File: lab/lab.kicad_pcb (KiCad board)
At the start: 2 copper layers, 45.7 x 31.8 mm, 42 parts, among them J1 FACE, J3 C?, Q1 Q_NPN_EBC, Q2 Q_NPN_EBC, Q3 Q_NPN_EBC, U1 LM324, U2 L78L33_TO92

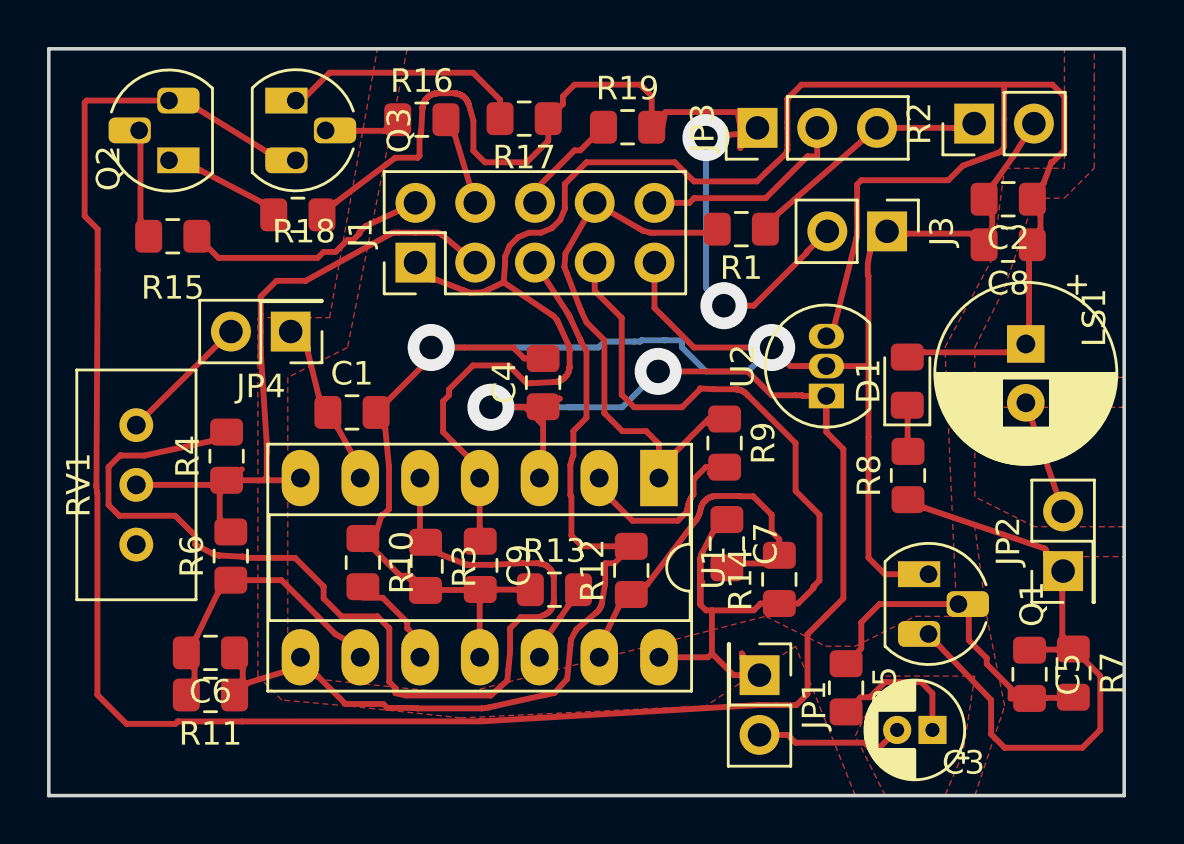
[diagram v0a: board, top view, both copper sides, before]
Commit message: Turned IC to bask
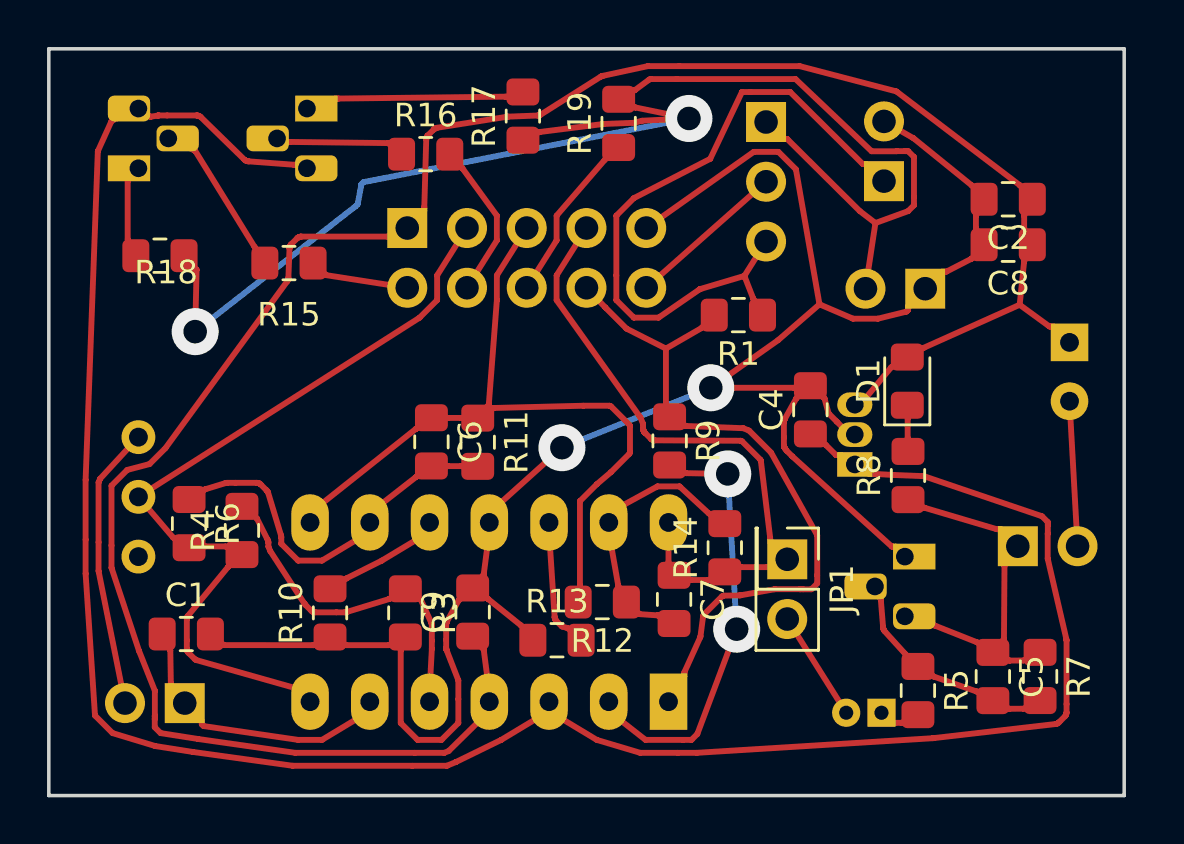
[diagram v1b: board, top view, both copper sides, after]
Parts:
- C3, J1, J3, JP2, JP3, JP4, LS1, Q1, Q2, Q3, R2, RV1, U1, U2: moved to B.Cu
- moved JP4 16.4 mm to (24.8, 45.6)
- moved R11 15.6 mm to (37.3, 34.5), turned to 270 degrees
- moved C6 13.0 mm to (35.3, 34.5), turned to 270 degrees
- moved C1 11.8 mm to (24.9, 42.7)
- moved C4 11.4 mm to (51.4, 33.1)
- moved U1 9.52 mm to (45.4, 45.5), turned to 90 degrees
- moved R18 6.12 mm to (23.8, 26.6)
- moved R15 5.07 mm to (29.3, 26.9)
- moved JP1 5.07 mm to (50.4, 39.5)
- moved R2 4.55 mm to (54.6, 23.4), turned to 0 degrees
- moved R1 3.66 mm to (48.4, 29.1)
- moved C7 3.26 mm to (45.6, 41.2)
- moved R4 3.23 mm to (27.3, 38.3)
- moved U2 3.15 mm to (53.3, 35.5)
- moved R5 3.06 mm to (56.0, 45.1)
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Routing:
- net Net-(R3-Pad1): track 43.9 -> 14.9 mm
- net CMEAS: track 45.0 -> 64.8 mm
- net TMEAS: track 10.6 -> 28.8 mm
- net SIN: track 41.7 -> 27.5 mm
- net Net-(C5-Pad1): track 27.2 -> 16.3 mm
- net Net-(R9-Pad2): track 8.65 -> 18.6 mm, vias 0 -> 2
- net +5V: track 86.3 -> 95.7 mm
- net 3V3: track 106.0 -> 97.9 mm, vias 2 -> 0
- net TRIANGLE: track 40.3 -> 32.9 mm
- net Net-(JP4-Pad2): track 5.66 -> 12.1 mm
- net CSD1: track 10.5 -> 4.24 mm
- net GNDD: track 85.9 -> 91.9 mm
- net SQUARE: track 29.3 -> 35.0 mm
- net Net-(C1-Pad1): track 7.06 -> 12.4 mm
- net Net-(C5-Pad2): track 14.1 -> 9.73 mm
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- removed copper zone on F.Cu, net +5V
- removed copper zone on F.Cu, net 3V3
- removed copper zone on F.Cu, net GNDD
- removed copper zone on F.Cu, net Net-(C3-Pad1)
- removed copper zone on F.Cu, net Net-(C5-Pad1)
- removed copper zone on F.Cu, net Net-(JP2-Pad2)

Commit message: Final PCB
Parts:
- moved R18 5.44 mm to (21.6, 21.6), turned to 270 degrees
- moved R8 3.95 mm to (59.5, 35.7)
- moved D1 3.40 mm to (58.9, 31.7)
- moved U2 3.39 mm to (56.7, 35.5)
- moved C4 1.98 mm to (53.4, 33.3)
- moved R9 1.57 mm to (43.9, 34.2)
- moved Q2 1.27 mm to (24.1, 22.9)
- moved R12 0.48 mm to (42.2, 41.1)
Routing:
- net CMEAS: track 64.8 -> 41.1 mm, vias 2 -> 0
- net TMEAS: track 28.8 -> 14.4 mm
- net +5V: track 95.7 -> 109.1 mm
- net Net-(R3-Pad1): track 14.9 -> 26.8 mm
- net SQUARE: track 35.0 -> 42.3 mm, vias 0 -> 2
- net 3V3: track 97.9 -> 91.3 mm, vias 0 -> 3
- net CSD1: track 4.24 -> 10.7 mm
- net TRIANGLE: track 32.9 -> 26.5 mm
- net GNDD: track 91.9 -> 98.3 mm, vias 2 -> 0
- net Net-(C7-Pad2): track 12.0 -> 16.3 mm
- net Net-(R9-Pad2): track 18.6 -> 14.7 mm, vias 2 -> 0
- net VREF3.3: track 30.0 -> 33.8 mm, vias 0 -> 2
- net Net-(C1-Pad1): track 12.4 -> 15.8 mm
- net MEAS: track 6.80 -> 10.2 mm
- net Net-(C5-Pad1): track 16.3 -> 13.3 mm
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- added copper zone on F.Cu, net +5V
- added copper zone on F.Cu, net 3V3
- added copper zone on F.Cu, net GNDD
- added copper zone on F.Cu, net TRIANGLE
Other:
- net class Default: clearance 0.2 -> 0.25; trace_width 0.25 -> 0.35; via_dia 2 -> 1.2; via_drill 1 -> 0.8
- rule trace_clearance: 0.2 -> 0.25

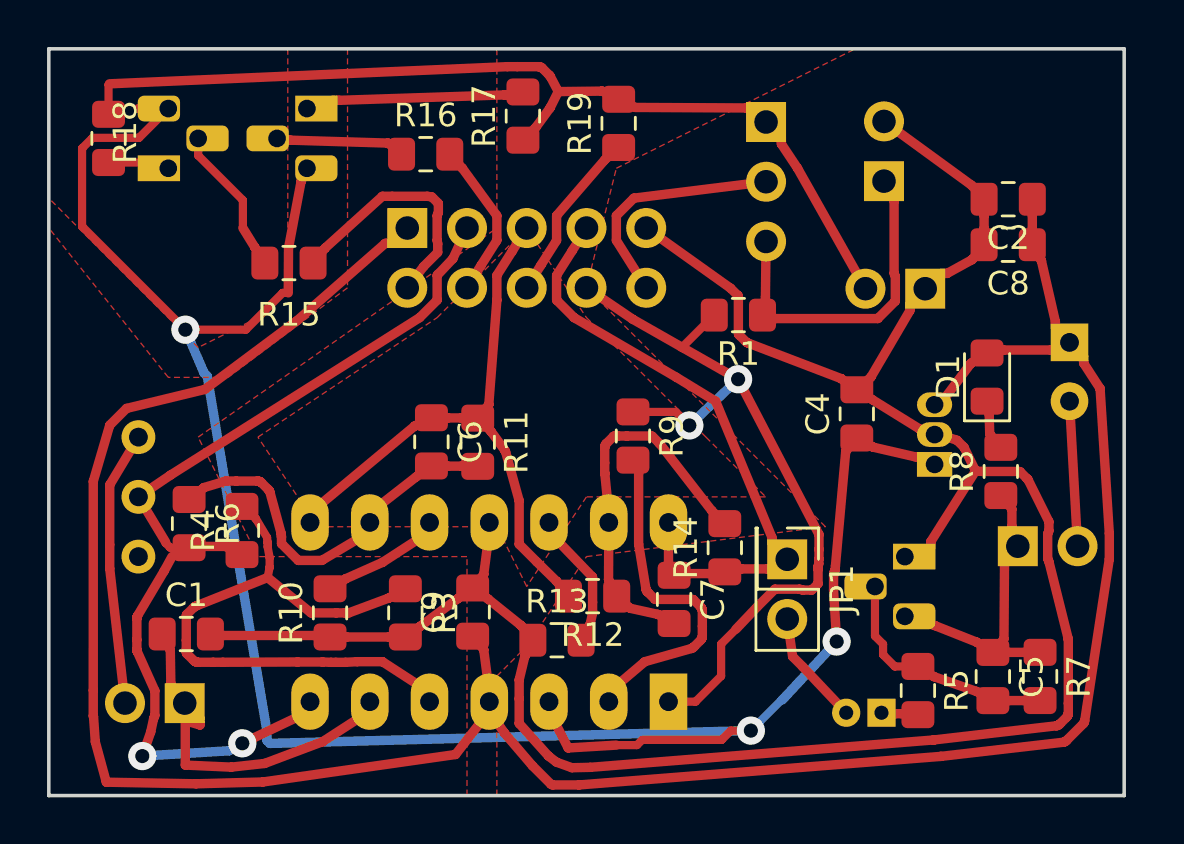
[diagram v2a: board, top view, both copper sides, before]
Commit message: Fill more space with Cu.
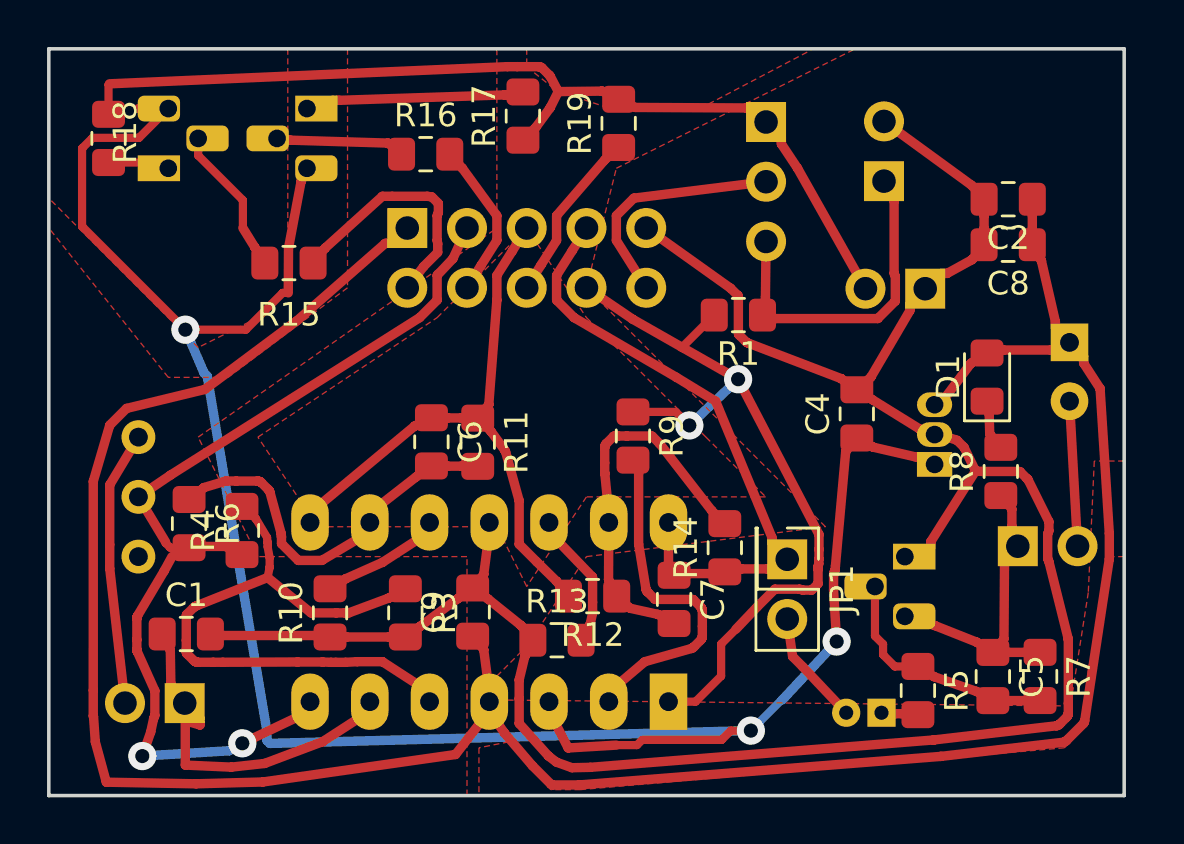
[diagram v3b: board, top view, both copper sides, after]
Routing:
- added copper zone on F.Cu, net CMEAS
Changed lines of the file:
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@@
       (pts
         (xy 38.1 45.72) (xy 38.1 44.45) (xy 39.37 43.18) (xy 41.91 39.37) (xy 52.07 38.1)
-        (xy 41.91 27.94) (xy 43.18 22.86) (xy 53.34 17.78) (xy 64.77 17.78) (xy 64.77 49.53)
-        (xy 38.1 49.53)
+        (xy 41.91 27.94) (xy 43.18 22.86) (xy 53.34 17.78) (xy 64.77 17.78) (xy 64.77 35.306)
+        (xy 63.5 35.306) (xy 63.246 40.894) (xy 62.484 45.72) (xy 38.1 45.466)
       )
     )
@@
       )
     )
+  )
+  (zone (net 3) (net_name +5V) (layer F.Cu) (hatch edge 0.508)
+    (connect_pads (clearance 0.508))
+    (min_thickness 0.254)
+    (fill yes (arc_segments 16) (thermal_gap 0.508) (thermal_bridge_width 0.508))
+    (polygon
+      (pts
+        (xy 64.77 44.196) (xy 64.77 39.37) (xy 64.262 39.37) (xy 63.246 44.196) (xy 62.992 46.736)
+        (xy 62.23 47.498) (xy 41.656 49.276) (xy 40.386 49.276) (xy 38.608 47.244) (xy 37.338 47.498)
+        (xy 37.338 49.53) (xy 64.77 49.53)
+      )
+    )
+  )
+  (zone (net 26) (net_name CMEAS) (layer F.Cu) (hatch edge 0.508)
+    (connect_pads (clearance 0.508))
+    (min_thickness 0.254)
+    (fill yes (arc_segments 16) (thermal_gap 0.508) (thermal_bridge_width 0.508))
+    (polygon
+      (pts
+        (xy 46.736 20.32) (xy 51.562 17.78) (xy 39.37 17.78) (xy 39.37 18.542) (xy 40.64 19.558)
+        (xy 42.926 20.32)
+      )
+    )

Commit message: Removed wrong parts. Remade PCB. Too thick.
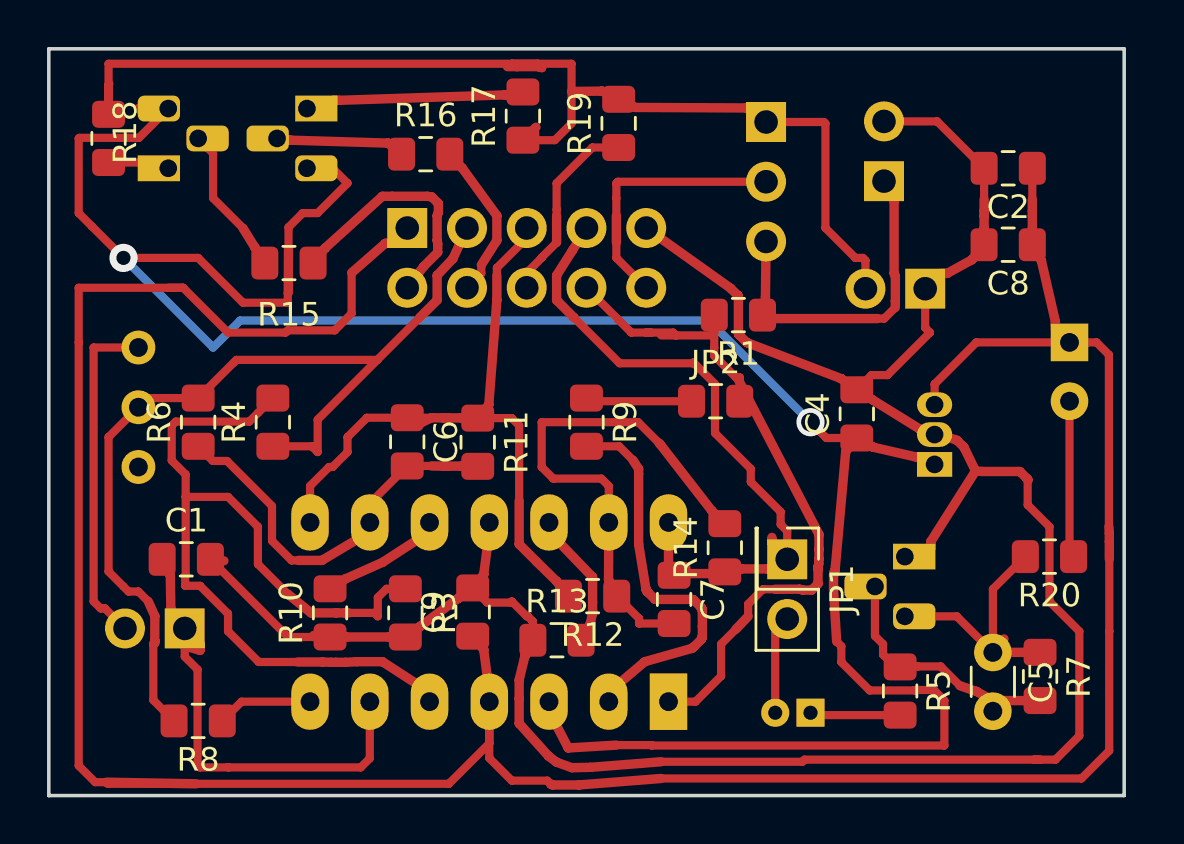
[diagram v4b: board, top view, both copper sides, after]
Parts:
- removed D1: LED, Diode_SMD:D_0805_2012Metric_Pad1.15x1.40mm_HandSolder
- added R20: 0R, Resistor_SMD:R_0805_2012Metric_Pad1.15x1.40mm_HandSolder, F.Cu at (61.6, 39.4)
- C5: footprint Capacitor_SMD:C_0805_2012Metric_Pad1.15x1.40mm_HandSolder -> Capacitor_THT:C_Disc_D3.0mm_W1.6mm_P2.50mm
- JP2: value SPK -> 0R; footprint Connector_PinHeader_2.54mm:PinHeader_2x01_P2.54mm_Vertical -> Resistor_SMD:R_0805_2012Metric_Pad1.15x1.40mm_HandSolder; moved to F.Cu
- R8: value 1K -> 0R
- moved R8 35.7 mm to (25.4, 46.4), turned to 180 degrees
- moved JP2 14.3 mm to (47.4, 32.8)
- moved R4 4.79 mm to (28.6, 33.7)
- moved R6 4.33 mm to (25.4, 33.7), turned to 90 degrees
- moved RV1 3.81 mm to (22.9, 30.5)
- moved C1 3.18 mm to (24.9, 39.5)
- moved JP4 3.17 mm to (24.8, 42.4)
- moved C3 3.02 mm to (51.4, 46.0)
- moved R9 2.06 mm to (41.9, 33.7)
- moved C2 1.32 mm to (59.8, 22.9)
- moved C6 1.03 mm to (34.3, 34.5)
- moved C5 1.02 mm to (59.2, 43.4)
- moved R5 0.76 mm to (55.2, 45.1)
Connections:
- JP2 pad 1: Net-(C5-Pad1) -> VREF3.3
- JP2 pad 2: Net-(JP2-Pad2) -> VREF3.3
- LS1 pad 2: Net-(JP2-Pad2) -> Net-(LS1-Pad2)
- R8 pad 1: Net-(C5-Pad1) -> SQUARE
- R8 pad 2: Net-(D1-Pad1) -> SQUARE
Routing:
- net +5V: track 109.1 -> 130.3 mm
- net Net-(R3-Pad1): track 26.8 -> 38.1 mm
- net CMEAS: track 41.1 -> 50.8 mm
- net 3V3: track 91.3 -> 100.9 mm, vias 3 -> 2
- net GNDD: track 98.3 -> 107.6 mm
- net Net-(LS1-Pad2): track 0.00 -> 6.68 mm
- net Net-(C7-Pad2): track 16.3 -> 22.7 mm
- net Net-(JP2-Pad2): track 6.17 -> 0.00 mm
- net Net-(C1-Pad1): track 15.8 -> 21.1 mm
- net TRIANGLE: track 26.5 -> 31.8 mm
- net Net-(C3-Pad1): track 1.55 -> 4.50 mm
- net Net-(JP4-Pad2): track 11.7 -> 14.5 mm
- net Net-(C6-Pad2): track 16.6 -> 19.3 mm
- net SIN: track 26.2 -> 28.9 mm
- net SQUARE: track 42.3 -> 45.0 mm, vias 2 -> 0
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- removed copper zone on F.Cu, net +5V
- removed copper zone on F.Cu, net 3V3
- removed copper zone on F.Cu, net CMEAS
- removed copper zone on F.Cu, net GNDD
- removed copper zone on F.Cu, net TRIANGLE

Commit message: Added thick tracks.
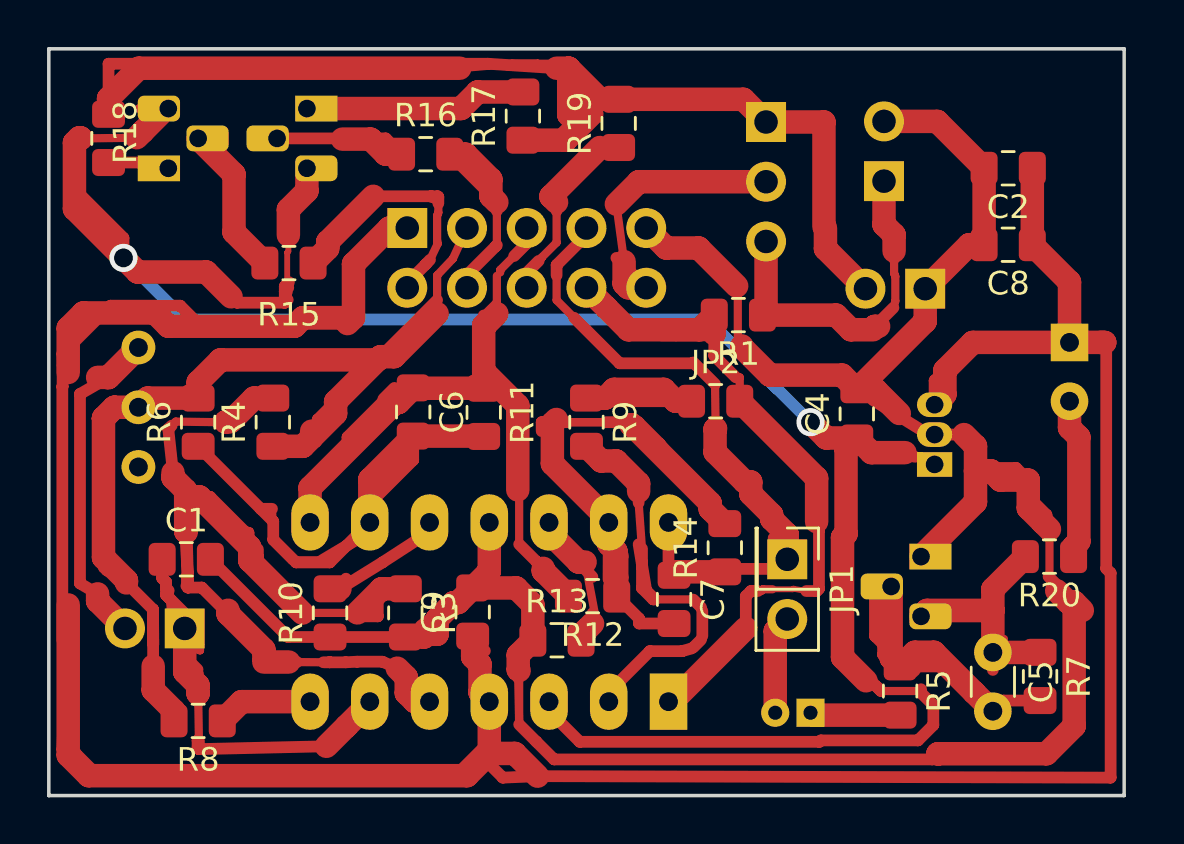
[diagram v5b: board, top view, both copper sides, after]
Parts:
- moved C6 1.30 mm to (34.5, 33.2)
- moved R11 1.30 mm to (37.5, 33.2)
- moved Q1 0.69 mm to (56.1, 39.4)
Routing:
- net CMEAS: track 50.8 -> 103.6 mm
- net +5V: track 130.3 -> 173.8 mm
- net SQUARE: track 45.0 -> 72.7 mm
- net Net-(R3-Pad1): track 38.1 -> 64.4 mm
- net TRIANGLE: track 31.8 -> 56.4 mm
- net GNDD: track 107.6 -> 127.9 mm
- net 3V3: track 100.9 -> 119.1 mm
- net Net-(C7-Pad2): track 22.7 -> 36.4 mm
- net Net-(C6-Pad2): track 19.3 -> 31.8 mm
- net VREF3.3: track 35.0 -> 46.6 mm
- net Net-(C5-Pad2): track 10.4 -> 21.8 mm
- net Net-(C5-Pad1): track 11.8 -> 22.5 mm
- net Net-(C1-Pad1): track 21.1 -> 28.6 mm
- net Net-(R13-Pad2): track 5.87 -> 11.5 mm
- net CSD2: track 6.81 -> 10.3 mm
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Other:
- net class infiltration added: clearance 0.25, trace_width 0.25, via_dia 1.2, via_drill 0.8
- rule via_min_drill: 0.3 -> 0.7
- rule via_min_size: 0.4 -> 1.2

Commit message: as of today
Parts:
- added C10: 100n, Capacitor_SMD:C_1206_3216Metric_Pad1.42x1.75mm_HandSolder, F.Cu at (39.4, 41.9)
- C1, C2, C4, C6, C7, C8: footprint Capacitor_SMD:C_0805_2012Metric_Pad1.15x1.40mm_HandSolder -> Capacitor_SMD:C_1206_3216Metric_Pad1.42x1.75mm_HandSolder
- JP2, R1, R11, R14, R15, R16, R17, R18, R19, R20, R4, R5, R6, R7, R8, R9: footprint Resistor_SMD:R_0805_2012Metric_Pad1.15x1.40mm_HandSolder -> Resistor_SMD:R_1206_3216Metric_Pad1.42x1.75mm_HandSolder
- R12, R3: footprint Resistor_SMD:R_0805_2012Metric_Pad1.15x1.40mm_HandSolder -> Resistor_SMD:R_0815_2038Metric_Pad1.53x4.00mm_HandSolder
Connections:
- U1 pad 11: GNDD -> -5V
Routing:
- net Net-(R13-Pad2): track 11.5 -> 4.53 mm
- net 3V3: track 119.1 -> 114.1 mm
- net GNDD: track 127.9 -> 124.8 mm
- net CMEAS: track 103.6 -> 101.9 mm
- net Net-(R9-Pad2): track 19.6 -> 18.6 mm
